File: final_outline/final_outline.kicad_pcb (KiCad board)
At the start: 2 copper layers, 99.8 x 101.8 mm, 2 parts, among them P001 CANCONNECTOR, P002 AUXCONNECTOR

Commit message: more template placements
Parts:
- added P100: ISP, Connectors_Molex:Connector_Microfit3_Header_02x03_Angled_43045-060x, F.Cu at (118.9, 34.8)
- added P101: DEBUG_LED, Connectors_Molex:Connector_Microfit3_Header_02x08_Angled_43045-160x, F.Cu at (166.3, 34.3)
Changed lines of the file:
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@@
-(kicad_pcb (version 4) (host pcbnew 4.0.0-rc1-stable)
+(kicad_pcb (version 4) (host pcbnew "(2015-09-17 BZR 6202)-product")
   (general
     (links 0)
     (no_connects 0)
-    (area 0 0 0 0)
+    (area 102.424999 25.824999 202.325001 127.825001)
     (thickness 1.6)
     (drawings 7)
     (tracks 0)
     (zones 0)
-    (modules 2)
-    (nets 32)
+    (modules 4)
+    (nets 54)
   )
   (page A4)
@@
   (net 30 "Net-(P002-Pad1)")
   (net 31 "Net-(P002-Pad9)")
+  (net 32 "Net-(P100-Pad1)")
+  (net 33 "Net-(P100-Pad4)")
+  (net 34 "Net-(P100-Pad5)")
+  (net 35 "Net-(P100-Pad2)")
+  (net 36 "Net-(P100-Pad6)")
+  (net 37 "Net-(P100-Pad3)")
+  (net 38 "Net-(P101-Pad9)")
+  (net 39 "Net-(P101-Pad1)")
+  (net 40 "Net-(P101-Pad2)")
+  (net 41 "Net-(P101-Pad10)")
+  (net 42 "Net-(P101-Pad11)")
+  (net 43 "Net-(P101-Pad3)")
+  (net 44 "Net-(P101-Pad4)")
+  (net 45 "Net-(P101-Pad12)")
+  (net 46 "Net-(P101-Pad13)")
+  (net 47 "Net-(P101-Pad5)")
+  (net 48 "Net-(P101-Pad6)")
+  (net 49 "Net-(P101-Pad14)")
+  (net 50 "Net-(P101-Pad15)")
+  (net 51 "Net-(P101-Pad7)")
+  (net 52 "Net-(P101-Pad16)")
+  (net 53 "Net-(P101-Pad8)")
   (net_class Default "This is the default net class."
     (clearance 0.2)
@@
     (add_net "Net-(P002-Pad8)")
     (add_net "Net-(P002-Pad9)")
-  )
-  (module MITEVT_AUTOMOTIVECON:776280-1 (layer F.Cu)
+    (add_net "Net-(P100-Pad1)")
+    (add_net "Net-(P100-Pad2)")
+    (add_net "Net-(P100-Pad3)")
+    (add_net "Net-(P100-Pad4)")
+    (add_net "Net-(P100-Pad5)")
+    (add_net "Net-(P100-Pad6)")
+    (add_net "Net-(P101-Pad1)")
+    (add_net "Net-(P101-Pad10)")
+    (add_net "Net-(P101-Pad11)")
+    (add_net "Net-(P101-Pad12)")
+    (add_net "Net-(P101-Pad13)")
+    (add_net "Net-(P101-Pad14)")
+    (add_net "Net-(P101-Pad15)")
+    (add_net "Net-(P101-Pad16)")
+    (add_net "Net-(P101-Pad2)")
+    (add_net "Net-(P101-Pad3)")
+    (add_net "Net-(P101-Pad4)")
+    (add_net "Net-(P101-Pad5)")
+    (add_net "Net-(P101-Pad6)")
+    (add_net "Net-(P101-Pad7)")
+    (add_net "Net-(P101-Pad8)")
+    (add_net "Net-(P101-Pad9)")
+  )
+  (module MITEVT_AUTOMOTIVECON:776280-1 locked (layer F.Cu)
     (at 120.75 122.25)
     (fp_text reference P001 (at 4 4) (layer F.SilkS)
@@
     (pad 10 thru_hole circle (at 14.5 -3.5) (size 2 2) (drill 2) (layers *.Cu *.Mask F.SilkS))
   )
-  (module MITEVT_AUTOMOTIVECON:776087-1 (layer F.Cu)
+  (module MITEVT_AUTOMOTIVECON:776087-1 locked (layer F.Cu)
     (at 158.496 114.25)
     (fp_text reference P002 (at 15 12) (layer F.SilkS)
@@
     (pad 24 thru_hole circle (at -6.5 4.5) (size 2.85 2.85) (drill 2.85) (layers *.Cu *.Mask F.SilkS))
   )
+  (module Connectors_Molex:Connector_Microfit3_Header_02x03_Angled_43045-060x (layer F.Cu)
+    (at 118.92 34.8 180)
+    (descr "Microfit 02x03 header angled 43045-0600")
+    (tags "Microfit 02x03 angled 3mm pitch")
+    (fp_text reference P100 (at -2 11 180) (layer F.SilkS)
+      (effects (font (size 1 1) (thickness 0.15)))
+    )
+    (fp_text value ISP (at -3 -6.604 180) (layer F.Fab)
+      (effects (font (size 1 1) (thickness 0.15)))
+    )
+    (fp_line (start -10.2 -4.55) (end -10.2 9.2) (layer F.CrtYd) (width 0.05))
+    (fp_line (start -10.2 9.2) (end 4.2 9.2) (layer F.CrtYd) (width 0.05))
+    (fp_line (start 4.2 9.2) (end 4.2 -4.55) (layer F.CrtYd) (width 0.05))
+    (fp_line (start 4.2 -4.55) (end -10.2 -4.55) (layer F.CrtYd) (width 0.05))
+    (fp_line (start -10 9) (end -10 -4.35) (layer F.SilkS) (width 0.15))
+    (fp_line (start -10 -4.35) (end 4 -4.35) (layer F.SilkS) (width 0.15))
+    (fp_line (start 4 -4.35) (end 4 9) (layer F.SilkS) (width 0.15))
+    (fp_line (start 4 9) (end -10 9) (layer F.SilkS) (width 0.15))
+    (pad 1 thru_hole circle (at 0 0 180) (size 1.5 1.5) (drill 1.1) (layers *.Cu *.Mask F.SilkS)
+      (net 32 "Net-(P100-Pad1)"))
+    (pad 4 thru_hole circle (at 0 -3 180) (size 1.5 1.5) (drill 1.1) (layers *.Cu *.Mask F.SilkS)
+      (net 33 "Net-(P100-Pad4)"))
+    (pad 5 thru_hole circle (at -3 -3 180) (size 1.5 1.5) (drill 1.1) (layers *.Cu *.Mask F.SilkS)
+      (net 34 "Net-(P100-Pad5)"))
+    (pad 2 thru_hole circle (at -3 0 180) (size 1.5 1.5) (drill 1.1) (layers *.Cu *.Mask F.SilkS)
+      (net 35 "Net-(P100-Pad2)"))
+    (pad 6 thru_hole circle (at -6 -3 180) (size 1.5 1.5) (drill 1.1) (layers *.Cu *.Mask F.SilkS)
+      (net 36 "Net-(P100-Pad6)"))
+    (pad 3 thru_hole circle (at -6 0 180) (size 1.5 1.5) (drill 1.1) (layers *.Cu *.Mask F.SilkS)
+      (net 37 "Net-(P100-Pad3)"))
+    (pad "" np_thru_hole circle (at -3 4.32 180) (size 3.1 3.1) (drill 3.1) (layers *.Cu *.Mask F.SilkS))
+  )
+  (module Connectors_Molex:Connector_Microfit3_Header_02x08_Angled_43045-160x (layer F.Cu)
+    (at 166.26 34.29 180)
+    (descr "Microfit 02x08 header angled 43045-1600")
+    (tags "Microfit 02x08 angled 3mm pitch")
+    (fp_text reference P101 (at -10 11 180) (layer F.SilkS)
+      (effects (font (size 1 1) (thickness 0.15)))
+    )
+    (fp_text value DEBUG_LED (at -10.5 -6.604 180) (layer F.Fab)
+      (effects (font (size 1 1) (thickness 0.15)))
+    )
+    (fp_line (start -25.2 -4.55) (end -25.2 9.2) (layer F.CrtYd) (width 0.05))
+    (fp_line (start -25.2 9.2) (end 4.2 9.2) (layer F.CrtYd) (width 0.05))
+    (fp_line (start 4.2 9.2) (end 4.2 -4.55) (layer F.CrtYd) (width 0.05))
+    (fp_line (start 4.2 -4.55) (end -25.2 -4.55) (layer F.CrtYd) (width 0.05))
+    (fp_line (start -25 9) (end -25 -4.35) (layer F.SilkS) (width 0.15))
+    (fp_line (start -25 -4.35) (end 4 -4.35) (layer F.SilkS) (width 0.15))
+    (fp_line (start 4 -4.35) (end 4 9) (layer F.SilkS) (width 0.15))
+    (fp_line (start 4 9) (end -25 9) (layer F.SilkS) (width 0.15))
+    (pad 9 thru_hole circle (at 0 -3 180) (size 1.5 1.5) (drill 1.1) (layers *.Cu *.Mask F.SilkS)
+      (net 38 "Net-(P101-Pad9)"))
+    (pad 1 thru_hole circle (at 0 0 180) (size 1.5 1.5) (drill 1.1) (layers *.Cu *.Mask F.SilkS)
+      (net 39 "Net-(P101-Pad1)"))
+    (pad 2 thru_hole circle (at -3 0 180) (size 1.5 1.5) (drill 1.1) (layers *.Cu *.Mask F.SilkS)
+      (net 40 "Net-(P101-Pad2)"))
+    (pad 10 thru_hole circle (at -3 -3 180) (size 1.5 1.5) (drill 1.1) (layers *.Cu *.Mask F.SilkS)
+      (net 41 "Net-(P101-Pad10)"))
+    (pad 11 thru_hole circle (at -6 -3 180) (size 1.5 1.5) (drill 1.1) (layers *.Cu *.Mask F.SilkS)
+      (net 42 "Net-(P101-Pad11)"))
+    (pad 3 thru_hole circle (at -6 0 180) (size 1.5 1.5) (drill 1.1) (layers *.Cu *.Mask F.SilkS)
+      (net 43 "Net-(P101-Pad3)"))
+    (pad 4 thru_hole circle (at -9 0 180) (size 1.5 1.5) (drill 1.1) (layers *.Cu *.Mask F.SilkS)
+      (net 44 "Net-(P101-Pad4)"))
+    (pad 12 thru_hole circle (at -9 -3 180) (size 1.5 1.5) (drill 1.1) (layers *.Cu *.Mask F.SilkS)
+      (net 45 "Net-(P101-Pad12)"))
+    (pad "" np_thru_hole circle (at -2.1 4.32 180) (size 3.1 3.1) (drill 3.1) (layers *.Cu *.Mask F.SilkS))
+    (pad 13 thru_hole circle (at -12 -3 180) (size 1.5 1.5) (drill 1.1) (layers *.Cu *.Mask F.SilkS)
+      (net 46 "Net-(P101-Pad13)"))
+    (pad 5 thru_hole circle (at -12 0 180) (size 1.5 1.5) (drill 1.1) (layers *.Cu *.Mask F.SilkS)
+      (net 47 "Net-(P101-Pad5)"))
+    (pad 6 thru_hole circle (at -15 0 180) (size 1.5 1.5) (drill 1.1) (layers *.Cu *.Mask F.SilkS)
+      (net 48 "Net-(P101-Pad6)"))
+    (pad 14 thru_hole circle (at -15 -3 180) (size 1.5 1.5) (drill 1.1) (layers *.Cu *.Mask F.SilkS)
+      (net 49 "Net-(P101-Pad14)"))
+    (pad 15 thru_hole circle (at -18 -3 180) (size 1.5 1.5) (drill 1.1) (layers *.Cu *.Mask F.SilkS)
+      (net 50 "Net-(P101-Pad15)"))
+    (pad 7 thru_hole circle (at -18 0 180) (size 1.5 1.5) (drill 1.1) (layers *.Cu *.Mask F.SilkS)
+      (net 51 "Net-(P101-Pad7)"))
+    (pad 16 thru_hole circle (at -21 -3 180) (size 1.5 1.5) (drill 1.1) (layers *.Cu *.Mask F.SilkS)
+      (net 52 "Net-(P101-Pad16)"))
+    (pad 8 thru_hole circle (at -21 0 180) (size 1.5 1.5) (drill 1.1) (layers *.Cu *.Mask F.SilkS)
+      (net 53 "Net-(P101-Pad8)"))
+    (pad "" np_thru_hole circle (at -18.8 4.32 180) (size 3.1 3.1) (drill 3.1) (layers *.Cu *.Mask F.SilkS))
+  )
   (dimension 99.50005 (width 0.3) (layer Cmts.User)

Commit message: New PCB layout
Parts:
- added C401: 10uF, Capacitors_SMD:C_0805_HandSoldering, F.Cu at (160.5, 154.6)
- added C402: 0.1uF, Capacitors_SMD:C_0603, F.Cu at (185.8, 154.5)
- added C403: 0.1uF, Capacitors_SMD:C_0603, F.Cu at (185.8, 148.6)
- added C404: 10uF, Capacitors_SMD:C_0805_HandSoldering, F.Cu at (171.5, 147.3)
- added C405: 0.1uF, Capacitors_SMD:C_0603_HandSoldering, F.Cu at (188.9, 142.7)
- added C406: 10uF, Capacitors_SMD:C_0805_HandSoldering, F.Cu at (177.6, 143.9)
- added C407: 0.1uF, Capacitors_SMD:C_0603_HandSoldering, F.Cu at (184.2, 142.7)
- added C408: 0.1uF, Capacitors_SMD:C_0603_HandSoldering, F.Cu at (189.3, 136.4)
- added C409: 1uF, Capacitors_SMD:C_0805_HandSoldering, F.Cu at (165.6, 154.6)
- added C410: 1uF, Capacitors_SMD:C_0805_HandSoldering, F.Cu at (184.4, 136.6)
- added C411: 1uF, Capacitors_SMD:C_0805_HandSoldering, F.Cu at (171.5, 153.6)
- added C412: 1uF, Capacitors_SMD:C_0805_HandSoldering, F.Cu at (176.5, 150.2)
- added R201: R, Resistors_SMD:R_0603_HandSoldering, F.Cu at (153.4, 164.2)
- added R301: 100, Resistors_SMD:R_0603_HandSoldering, F.Cu at (209.3, 142.3)
- added R302: 100, Resistors_SMD:R_0603_HandSoldering, F.Cu at (213.8, 136.4)
- added R303: 100, Resistors_SMD:R_0603_HandSoldering, F.Cu at (213.8, 142.3)
- added R304: 100, Resistors_SMD:R_0603_HandSoldering, F.Cu at (204.9, 142.3)
- added R305: 100, Resistors_SMD:R_0603_HandSoldering, F.Cu at (209.3, 136.4)
- added R306: 100, Resistors_SMD:R_0603_HandSoldering, F.Cu at (204.9, 136.4)
- added R307: 100, Resistors_SMD:R_0603_HandSoldering, F.Cu at (200.4, 142.3)
- added R308: 100, Resistors_SMD:R_0603_HandSoldering, F.Cu at (200.4, 136.4)
- added R401: 10k, Resistors_SMD:R_0603_HandSoldering, F.Cu at (181.3, 150.0)
- added R402: 10k, Resistors_SMD:R_0603_HandSoldering, F.Cu at (190.4, 148.6)
- added U401: ISO1050, Housings_SSOP:MSOP-8_3x3mm_Pitch0.65mm, F.Cu at (178.5, 137.1)
- added U402: ISO1050, Housings_SSOP:MSOP-8_3x3mm_Pitch0.65mm, F.Cu at (165.5, 147.8)
- added U403: LPC11C14, Housings_QFP:LQFP-48_7x7mm_Pitch0.5mm, F.Cu at (156.6, 140.5)
- added U404: MCP2515_TSSOP, Housings_SSOP:TSSOP-20_4.4x6.5mm_Pitch0.65mm, F.Cu at (168.6, 138.8)
- added U405: ISO1050, Housings_SSOP:MSOP-8_3x3mm_Pitch0.65mm, F.Cu at (154.6, 151.2)
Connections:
- net Net-(P100-Pad1) renamed /FRONT_PANEL/+5V
- net Net-(P100-Pad2) renamed /FRONT_PANEL/RXD
- net Net-(P100-Pad3) renamed /FRONT_PANEL/TXD
- net Net-(P100-Pad4) renamed /FRONT_PANEL/MCU_RESET_N
- net Net-(P100-Pad5) renamed /FRONT_PANEL/MCU_PROG_N
- P001 pad 2: Net-(P001-Pad2) -> Net-(P001-Pad1)
- P001 pad 3: Net-(P001-Pad3) -> /BACK_PANEL/CANH
- P001 pad 4: Net-(P001-Pad4) -> /BACK_PANEL/CANH
- P001 pad 5: Net-(P001-Pad5) -> GND
- P001 pad 6: Net-(P001-Pad6) -> GND
- P001 pad 8: Net-(P001-Pad8) -> Net-(P001-Pad7)
- P100 pad 6: Net-(P100-Pad6) -> GND
- P101 pad 1: Net-(P101-Pad1) -> GND
- P101 pad 11: Net-(P101-Pad11) -> GND
- P101 pad 13: Net-(P101-Pad13) -> GND
- P101 pad 15: Net-(P101-Pad15) -> GND
- P101 pad 3: Net-(P101-Pad3) -> GND
- P101 pad 5: Net-(P101-Pad5) -> GND
- P101 pad 7: Net-(P101-Pad7) -> GND
- P101 pad 9: Net-(P101-Pad9) -> GND

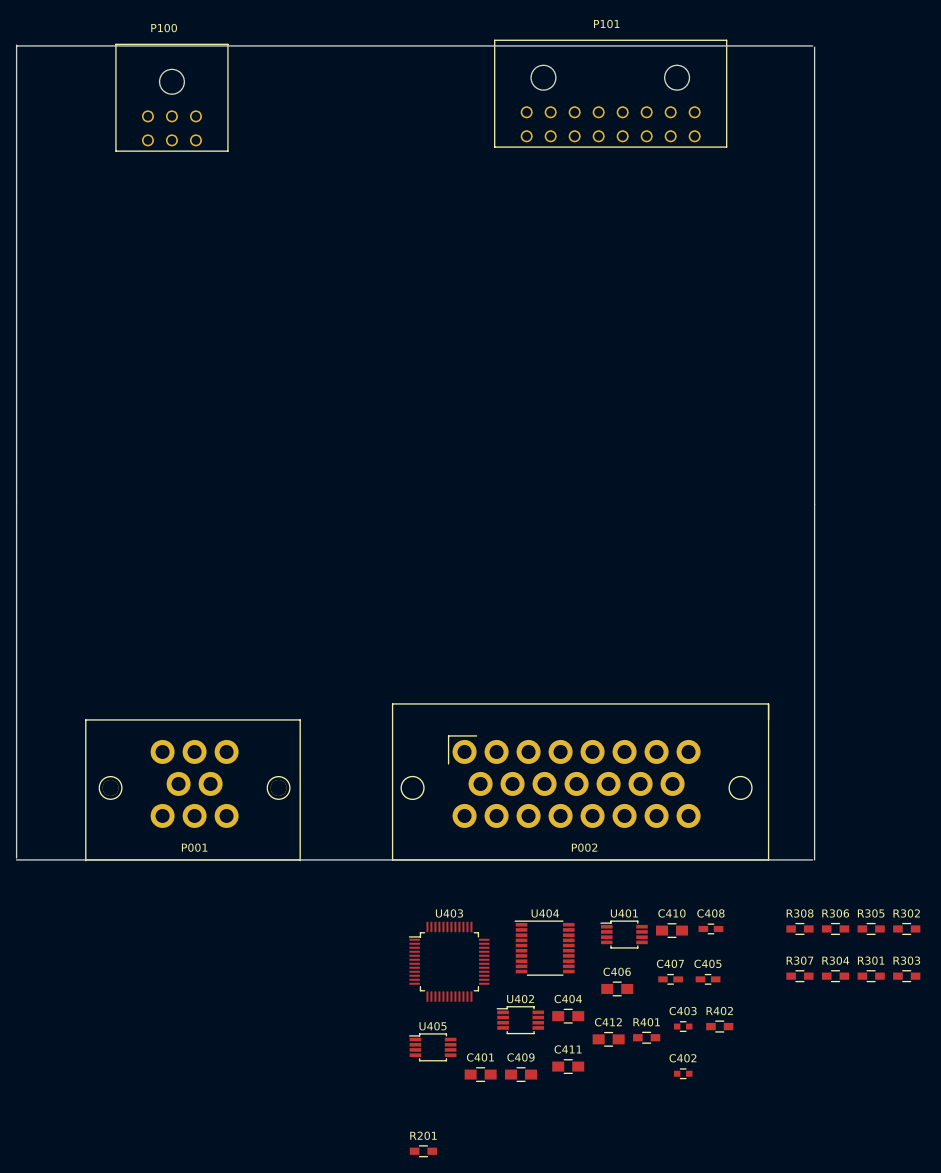
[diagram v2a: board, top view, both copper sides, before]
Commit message: Working on connections between sheets, deleted CAN2
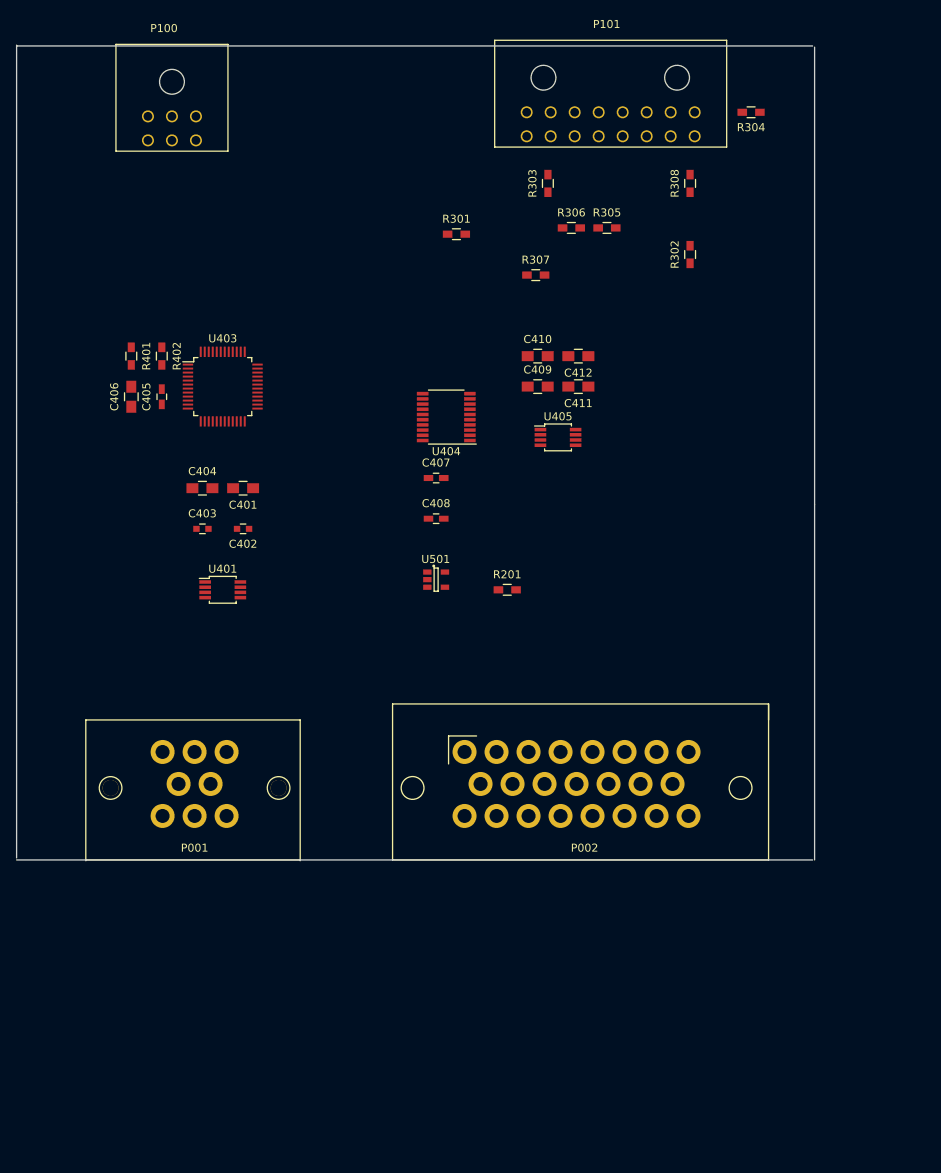
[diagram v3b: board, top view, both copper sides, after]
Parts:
- removed U402: ISO1050, Housings_SSOP:MSOP-8_3x3mm_Pitch0.65mm
- added U501: MCP1755, Housings_SOT-23_SOT-143_TSOT-6:SOT-23-5, F.Cu at (154.9, 92.7)
- moved R402 109.0 mm to (120.7, 64.8), turned to 270 degrees
- moved R303 108.8 mm to (168.9, 43.2), turned to 90 degrees
- moved R304 108.5 mm to (194.3, 34.3), turned to 180 degrees
- moved R401 106.8 mm to (116.8, 64.8), turned to 270 degrees
- moved R301 106.2 mm to (157.5, 49.5)
- moved C405 99.8 mm to (120.7, 69.8), turned to 90 degrees
- moved C406 95.8 mm to (116.8, 69.8), turned to 90 degrees
- moved R308 94.2 mm to (186.7, 43.2), turned to 90 degrees
- moved R306 93.6 mm to (171.8, 48.7)
- moved R305 93.6 mm to (176.3, 48.7)
- moved R307 93.6 mm to (167.4, 54.6)
- moved R302 88.5 mm to (186.7, 52.1), turned to 90 degrees
- moved C402 87.6 mm to (130.8, 86.4), turned to 180 degrees
- moved C403 86.5 mm to (125.7, 86.4)
- moved C409 86.0 mm to (167.6, 68.6)
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
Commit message: fixed metric-imperail problems
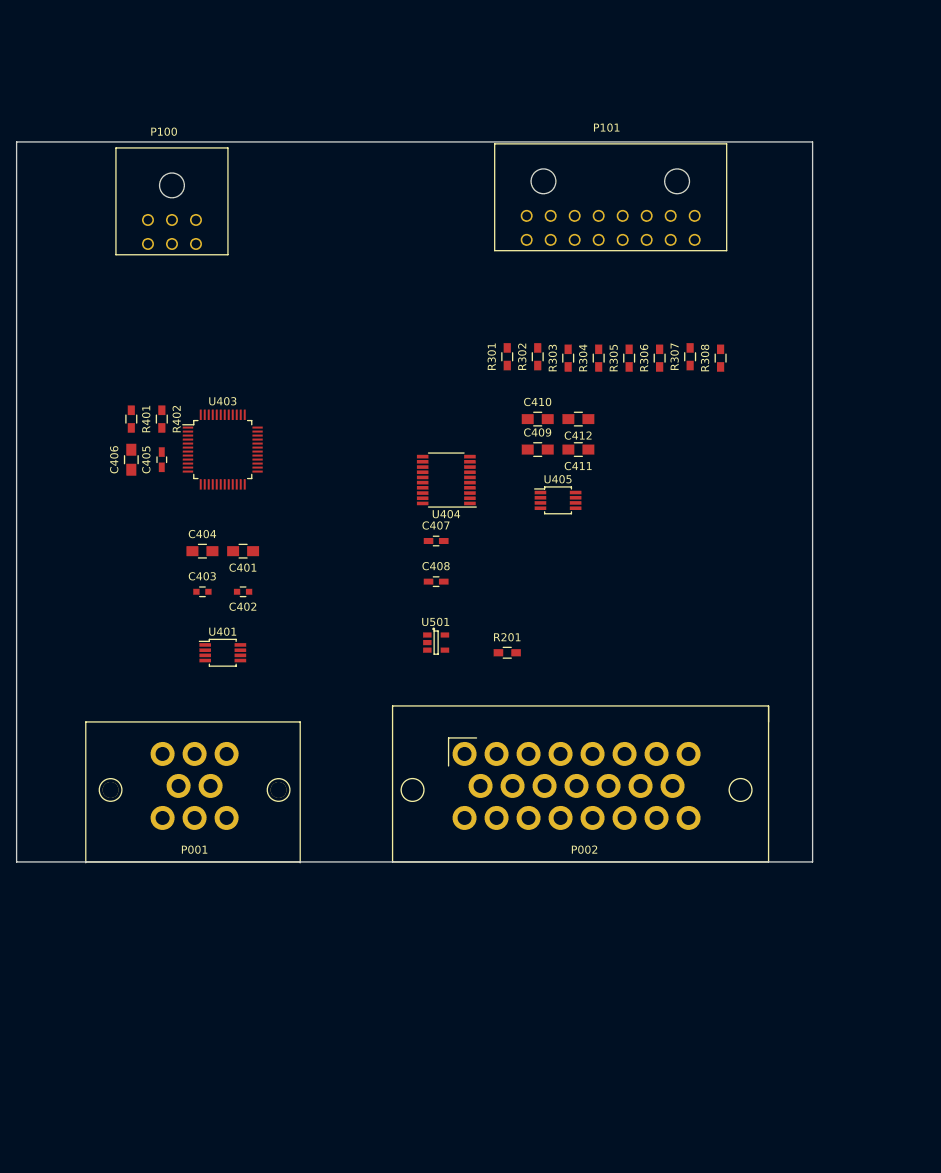
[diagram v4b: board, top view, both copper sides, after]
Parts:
- moved R304 36.2 mm to (175.3, 65.0), turned to 90 degrees
- moved R302 22.9 mm to (167.6, 64.8)
- moved R308 22.2 mm to (190.5, 65.0)
- moved R303 22.0 mm to (171.4, 65.0)
- moved R307 21.8 mm to (186.7, 64.8), turned to 90 degrees
- moved R306 19.7 mm to (182.9, 65.0), turned to 90 degrees
- moved R301 16.6 mm to (163.8, 64.8), turned to 90 degrees
- moved R305 16.5 mm to (179.1, 65.0), turned to 90 degrees
- moved P100 13.0 mm to (118.9, 47.8)
- moved P101 13.0 mm to (166.3, 47.2)
- moved C401 7.87 mm to (130.8, 89.2)
- moved C402 7.87 mm to (130.8, 94.2)
- moved C403 7.87 mm to (125.7, 94.2)
- moved C404 7.87 mm to (125.7, 89.2)
- moved C405 7.87 mm to (120.7, 77.7)
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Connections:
- C401 pad 1: /Micro_Controller/CAN1P -> /BACK_PANEL/CANH
- C402 pad 1: /Micro_Controller/CAN1P -> /BACK_PANEL/CANH
- C403 pad 1: +3V3 -> /Micro_Controller/+3V3
- C404 pad 1: +3V3 -> /Micro_Controller/+3V3
- C405 pad 1: +3V3 -> /Micro_Controller/+3V3
- C406 pad 1: +3V3 -> /Micro_Controller/+3V3
- R401 pad 1: +3V3 -> /Micro_Controller/+3V3
- R401 pad 2: /Micro_Controller/MCU_RESET_N -> /FRONT_PANEL/MCU_RESET_N
- R402 pad 1: +3V3 -> /Micro_Controller/+3V3
- R402 pad 2: /Micro_Controller/MCU_RESET_N -> /FRONT_PANEL/MCU_PROG_N
- U401 pad 1: +3V3 -> /Micro_Controller/+3V3
- U401 pad 6: /Micro_Controller/CAN1L -> GND
- U401 pad 7: /Micro_Controller/CAN1H -> /BACK_PANEL/CANH
- U401 pad 8: /Micro_Controller/CAN1P -> /BACK_PANEL/CANH
- U403 pad 1: /Micro_Controller/LED1 -> /FRONT_PANEL/LED1
- U403 pad 11: /Micro_Controller/LED2 -> /FRONT_PANEL/LED2
- U403 pad 12: /Micro_Controller/LED3 -> /FRONT_PANEL/LED3
- U403 pad 3: /Micro_Controller/MCU_RESET_N -> /FRONT_PANEL/MCU_RESET_N
- U403 pad 36: /Micro_Controller/LED4 -> /FRONT_PANEL/LED4
- U403 pad 37: /Micro_Controller/LED5 -> /FRONT_PANEL/LED5
- U403 pad 4: /Micro_Controller/MCU_RESET_N -> /FRONT_PANEL/MCU_PROG_N
- U403 pad 43: /Micro_Controller/LED6 -> /FRONT_PANEL/LED6
- U403 pad 44: +3V3 -> /Micro_Controller/+3V3
- U403 pad 46: /Micro_Controller/RXD -> /FRONT_PANEL/RXD
- U403 pad 47: /Micro_Controller/TXD -> /FRONT_PANEL/TXD
- U403 pad 48: /Micro_Controller/LED7 -> /FRONT_PANEL/LED7
- U403 pad 8: +3V3 -> /Micro_Controller/+3V3
- U403 pad 9: /Micro_Controller/LED0 -> /FRONT_PANEL/LED0
- U501 pad 1: /Power_Supplies/+5V -> /FRONT_PANEL/+5V
- U501 pad 3: /Power_Supplies/+5V -> /FRONT_PANEL/+5V
- U501 pad 5: /Power_Supplies/+3V3 -> /Micro_Controller/+3V3
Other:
- board size 99.8 x 101.8 mm -> 99.5 x 90 mm
